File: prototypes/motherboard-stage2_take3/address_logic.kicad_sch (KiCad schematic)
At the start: 11 parts, among them U23 GAL 22V10, U24 74LS670, U25 74LS670, U26 GAL 22V10, U27 GAL16V8

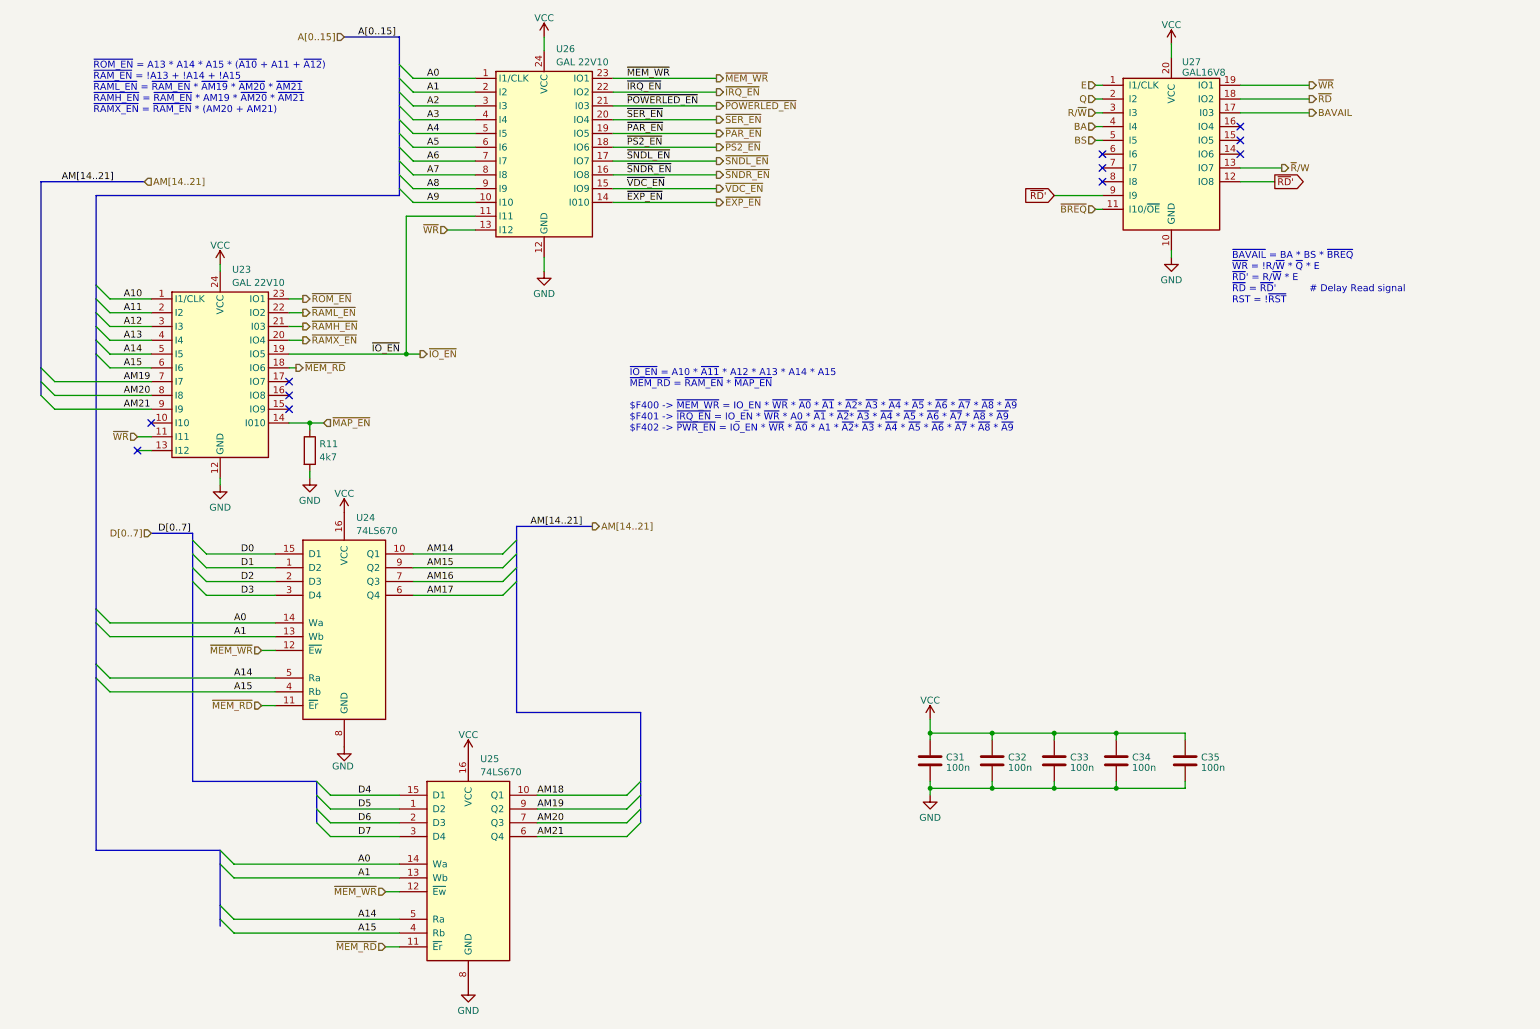
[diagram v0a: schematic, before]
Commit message: MMU read capability added
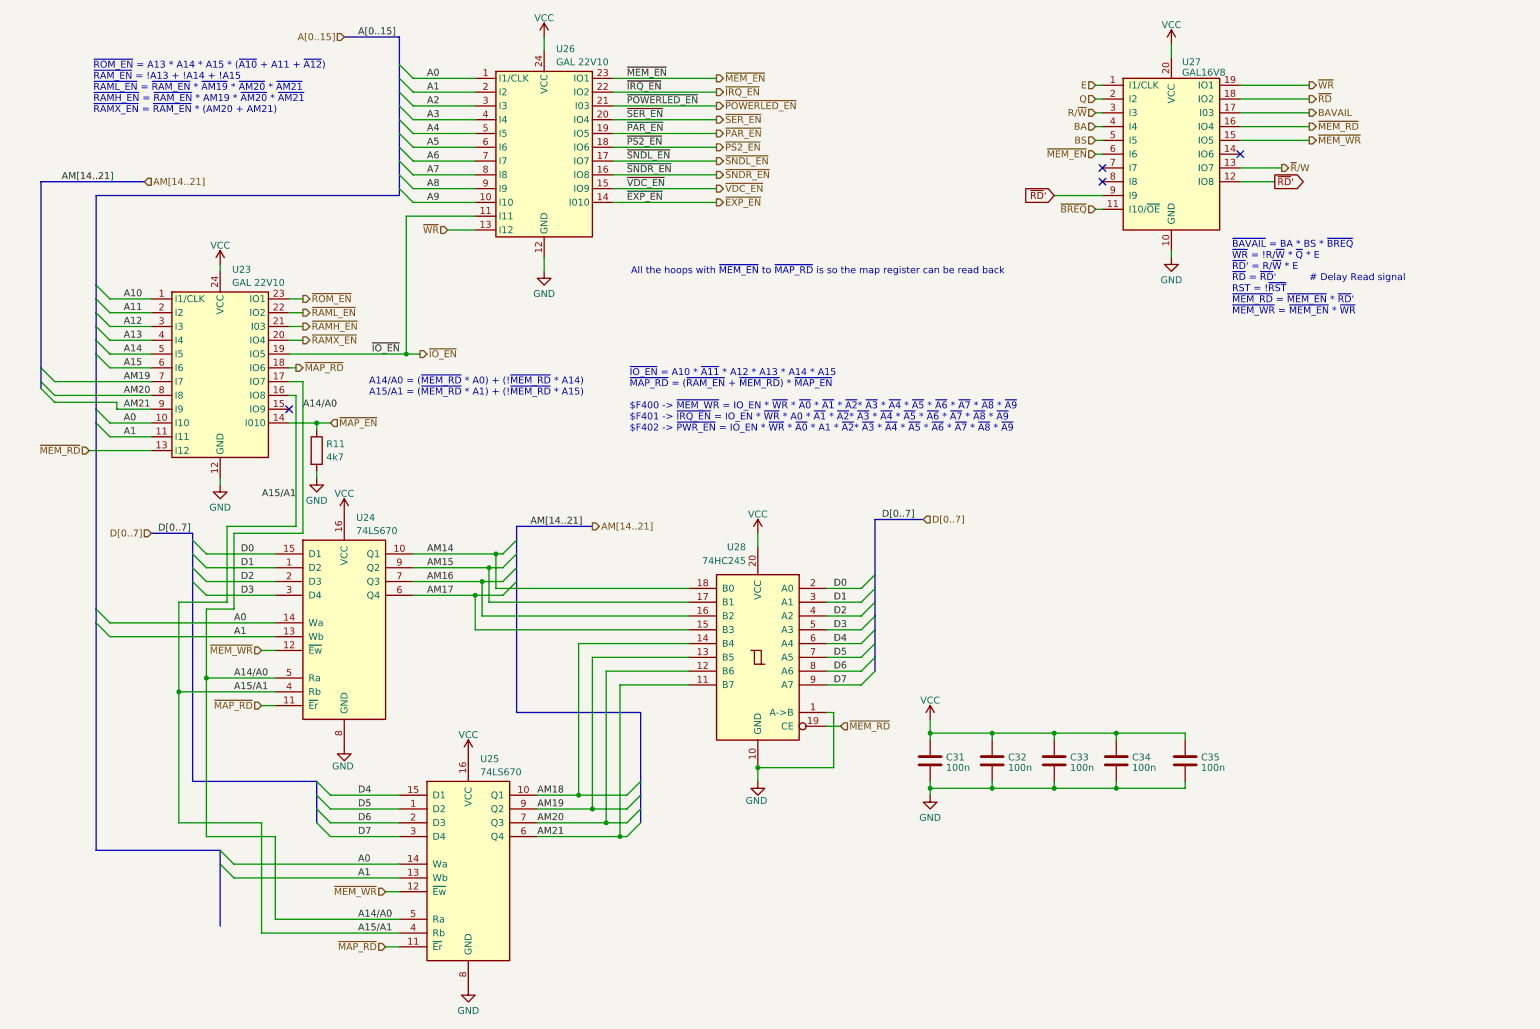
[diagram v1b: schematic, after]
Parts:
- added U28: 74HC245, symbol 74xx:74HC245
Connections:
- net A0: now also U23.10 (I10)
- net A1: now also U23.11 (I11)
- net A14: no longer U24.5 (Ra), U25.5 (Ra)
- net A15: no longer U24.4 (Rb), U25.4 (Rb)
- net AM14: now also U28.18 (B0)
- net AM15: now also U28.17 (B1)
- net AM16: now also U28.16 (B2)
- net AM17: now also U28.15 (B3)
- net AM18: now also U28.14 (B4)
- net AM19: now also U28.13 (B5)
- net AM20: now also U28.12 (B6)
- net AM21: now also U28.11 (B7)
- net D0: now also U28.2 (A0)
- net D1: now also U28.3 (A1)
- net D2: now also U28.4 (A2)
- net D3: now also U28.5 (A3)
- net D4: now also U28.6 (A4)
- net D5: now also U28.7 (A5)
- net D6: now also U28.8 (A6)
- net D7: now also U28.9 (A7)
- net GND: now also U28.1 (A->B), U28.10 (GND)
- net VCC: now also U28.20 (VCC)
- net ~{MEM_RD}: now also U23.13 (I12), U27.16 (IO4), U28.19 (CE); no longer U23.18 (IO6), U24.11 (~{Er}), U25.11 (~{Er})
- net ~{MEM_WR}: now also U27.15 (IO5); no longer U26.23 (IO1)
- net ~{WR}: no longer U23.11 (I11)
- net ~{MEM_EN}: now reaches U27.6 (I6)
- net ~{MEM_EN}: now also U26.23 (IO1)
- net A15/A1: now reaches U23.16 (IO8)
- net A15/A1: now also U24.4 (Rb), U25.4 (Rb)
- net A14/A0: now reaches U23.17 (IO7)
- net A14/A0: now also U24.5 (Ra), U25.5 (Ra)
- new net ~{MAP_RD}: U23.18 (IO6), U24.11 (~{Er}), U25.11 (~{Er})
- no-connect marks 11 -> 4
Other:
- note added: "A14/A0 = (~{MEM_RD} * A0) + (!~{MEM_RD} * A14) A15/A1 = (~{MEM_RD} * A1) + (!~{MEM_RD} * A15)"
- note added: "All the hoops with ~{MEM_EN} to ~{MAP_RD} is so the map register can be read back"
- note added: "~{BAVAIL} = BA * BS * ~{BREQ} ~{WR} = !R/~{W} * ~{Q} * E ~{RD}' = R/~{W} * E ~{RD} = ~{RD}' # Delay Read signal RST = !~{RST} ~{MEM_RD} = ~{MEM_EN} * ~{RD}' ~{MEM_WR} = ~{MEM_EN} * ~{WR}"
- note added: "~{IO_EN} = A10 * ~{A11} * A12 * A13 * A14 * A15 ~{MAP_RD} = (~{RAM_EN} + ~{MEM_RD}) * ~{MAP_EN} $F400 -> ~{MEM_WR} = IO_EN * ~{WR} * ~{A0} * ~{A1} * ~{A2}* ~{A3} * ~{A4} * ~{A5} * ~{A6} * ~{A7} * ~{A8} * ~{A9} $F401 -> ~{IRQ_EN} = IO_EN * ~{WR} * A0 * ~{A1} * ~{A2}* ~{A3} * ~{A4} * ~{A5} * ~{A6} * ~{A7} * ~{A8} * ~{A9} $F402 -> ~{PWR_EN} = IO_EN * ~{WR} * ~{A0} * A1 * ~{A2}* ~{A3} * ~{A4} * ~{A5}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"
- note removed: "~{BAVAIL} = BA * BS * ~{BREQ} ~{WR} = !R/~{W} * ~{Q} * E ~{RD}' = R/~{W} * E ~{RD} = ~{RD}' # Delay Read signal RST = !~{RST}"
- note removed: "~{IO_EN} = A10 * ~{A11} * A12 * A13 * A14 * A15 ~{MEM_RD} = ~{RAM_EN} * ~{MAP_EN} $F400 -> ~{MEM_WR} = IO_EN * ~{WR} * ~{A0} * ~{A1} * ~{A2}* ~{A3} * ~{A4} * ~{A5} * ~{A6} * ~{A7} * ~{A8} * ~{A9} $F401 -> ~{IRQ_EN} = IO_EN * ~{WR} * A0 * ~{A1} * ~{A2}* ~{A3} * ~{A4} * ~{A5} * ~{A6} * ~{A7} * ~{A8} * ~{A9} $F402 -> ~{PWR_EN} = IO_EN * ~{WR} * ~{A0} * A1 * ~{A2}* ~{A3} * ~{A4} * ~{A5} * ~{A6} * ~{A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"
- moved on the sheet: R11

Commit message: Started layout of board with mmu read register
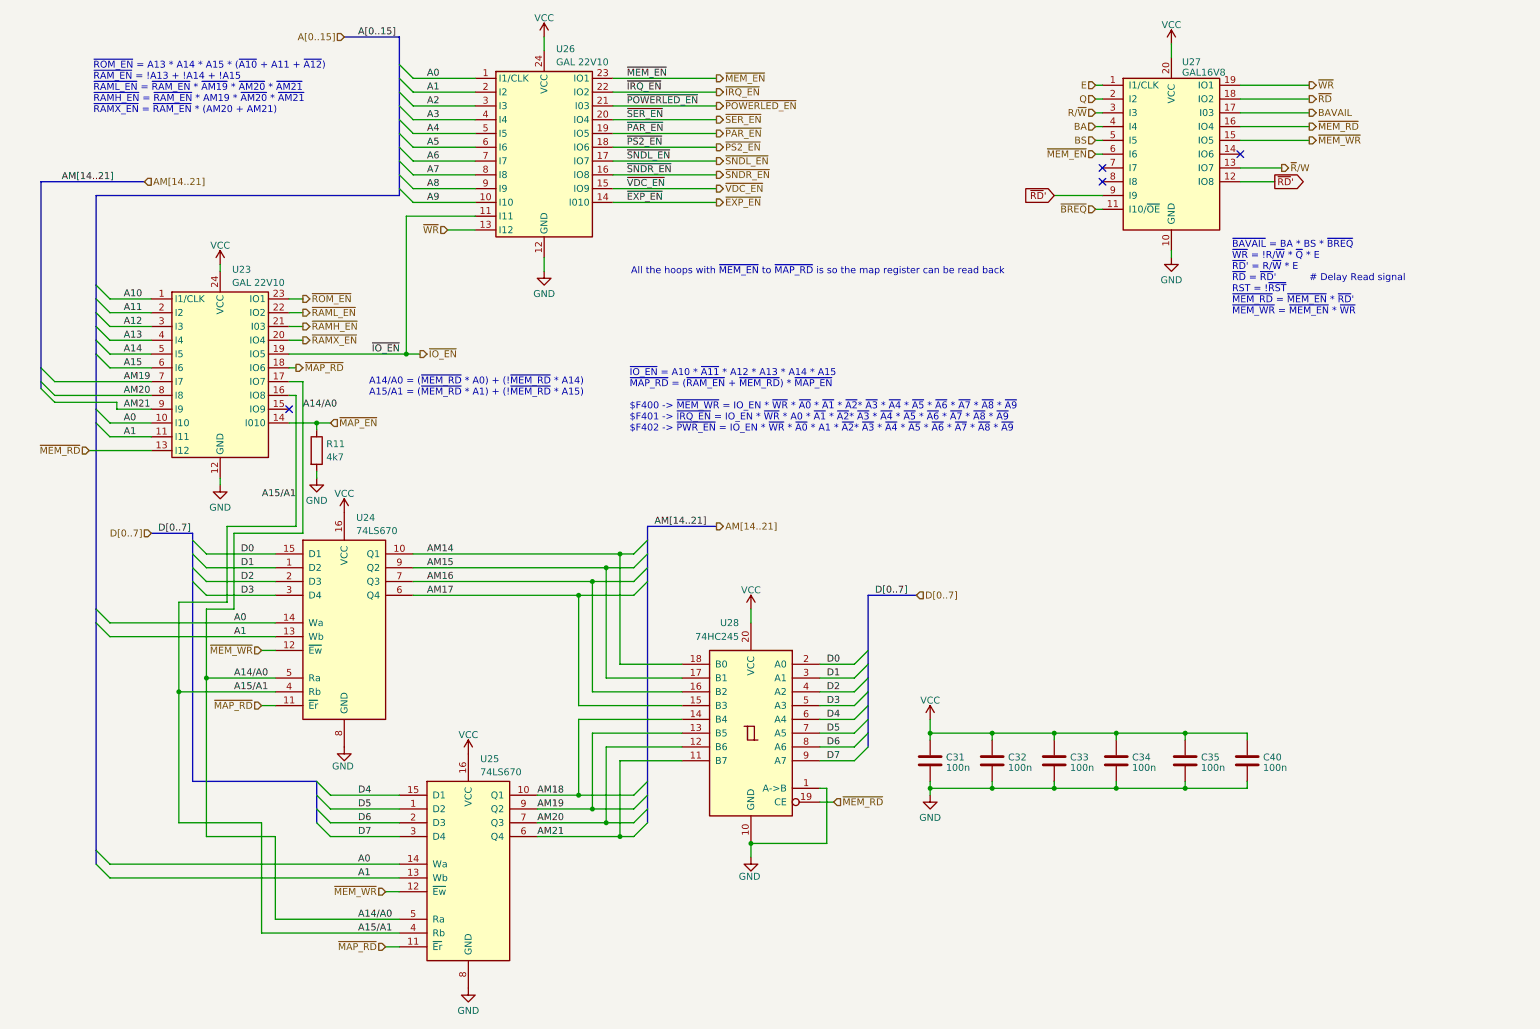
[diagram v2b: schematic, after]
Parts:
- added C40: 100n, Capacitor_THT:C_Disc_D5.0mm_W2.5mm_P2.50mm, symbol Device:C
- U28: footprint (none) -> Package_DIP:DIP-20_W7.62mm_Socket
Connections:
- net GND: now also C40.2
- net VCC: now also C40.1
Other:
- moved on the sheet: U28

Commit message: Finalized stage 2
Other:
- moved on the sheet: C31, C32, C33, C34, C35, C40
